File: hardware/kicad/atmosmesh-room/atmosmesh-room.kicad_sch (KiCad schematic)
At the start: 32 parts, among them U1 IDEASPARK_ESP32_1V14_TFT_30PIN

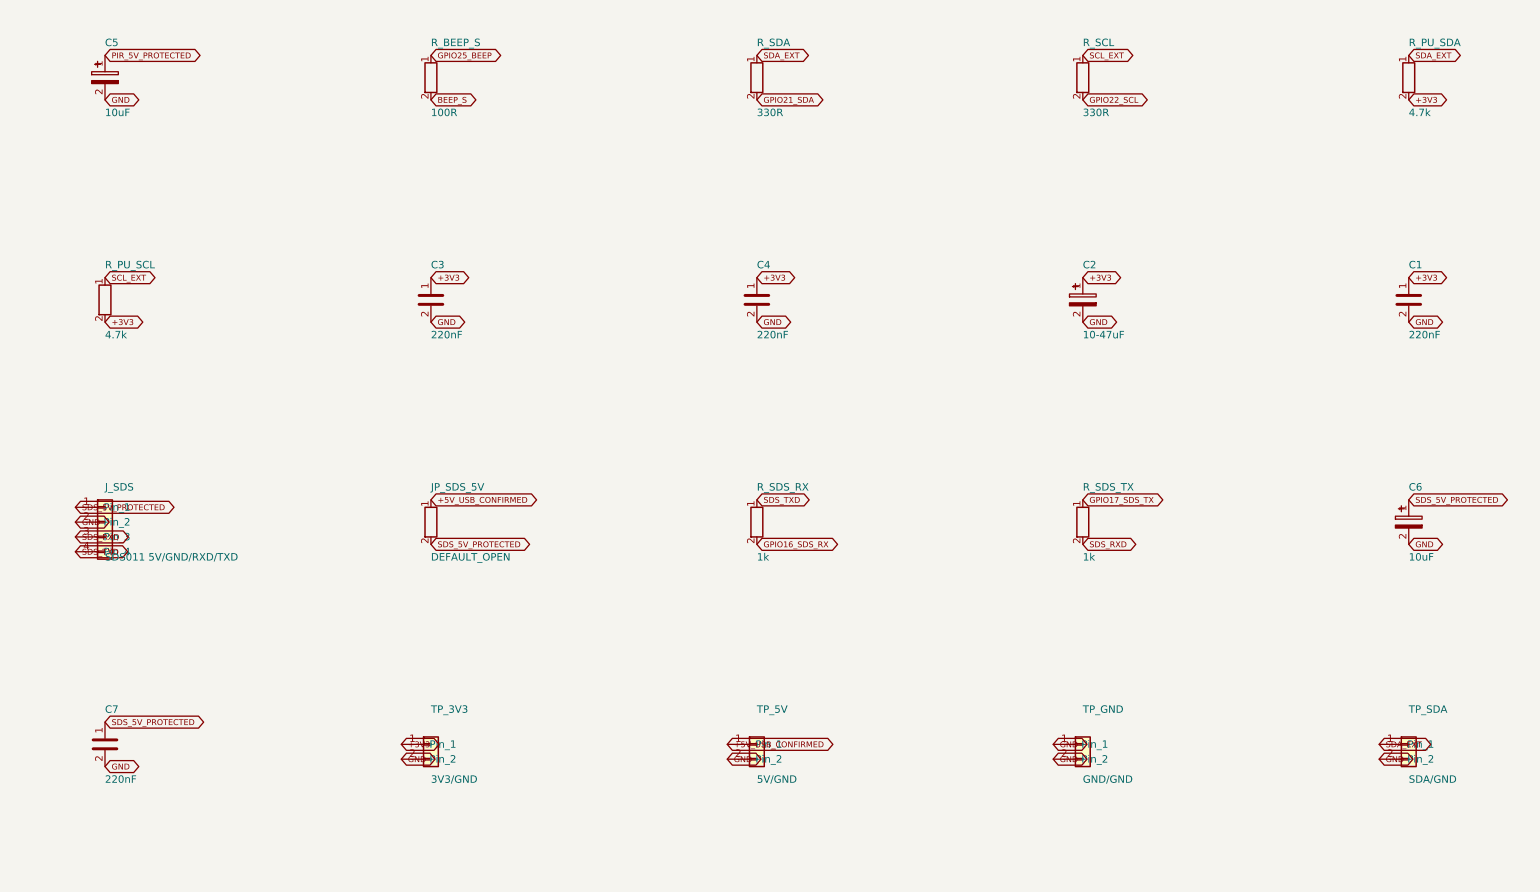
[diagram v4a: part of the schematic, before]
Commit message: :sparkles: feat(room): build on the perfboard and with the parts that exist
ROOM-03 and ROOM-04. The operator solders this by hand on a 31x27 perfboard and
does not need the PCB, and the inventory landed in the repo, so several values
that were chosen "because those parts are available" no longer have to be.

Perfboard becomes the build target (D-027):

- perfboard.md carries the grid facts, placement zones, hole budget and build
  order. The 7x9 cm label and the 31x27 hole count are reconciled: the extra
  millimetres are unholed lead-in strips.
- validate_room_perfboard.py gates it. A build plan with no gate is exactly the
  pattern this repo keeps hitting. All five assertions are mutation-proved.
- Step 1 is a dry-fit. 25.4 mm is exactly 10 pitches, so counting holes settles
  the row spacing that has blocked D-024 since the design started.
- The principal new hazard is orientation: the pinout sheet is a top view and
  soldering happens from the copper side, where left and right invert. Two
  connector orders were already found reversed here, so the wiring table is
  authoritative by pin NAME and the validator refuses to let that warning go.
- atmosmesh-room.kicad_pcb is parked, not deleted. It still cross-checks nets
  and silkscreen; it is not a fabrication candidate.

Values, now that stock is known:

- Pull-ups 4.7k -> 3.3k. Rise time binds on hand-wired perfboard: at 100 kHz
  I2C allows 1000 ns and 4.7k against ~200 pF gives 940 ns, on the limit. 3.3k
  gives 660 ns. wiring.md gains a table justifying every resistor; the operator
  holds a full E24 kit, so none of them is a stock compromise.
- C6 10uF -> 470uF. Its ripple limit is 20 mV against a fan and 10 uF was never
  shown to meet it. C5 and C2 -> 100uF. Electrolytics run to 1000 uF.
- Ceramics go the other way: 220nF -> 100nF for C1/C3/C4/C7, because the
  ceramic assortment stops at 100 nF and D-022 already allowed 47-220 nF.
- Closing JP_SDS_5V now has an ordering rule: before USB power, not while l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
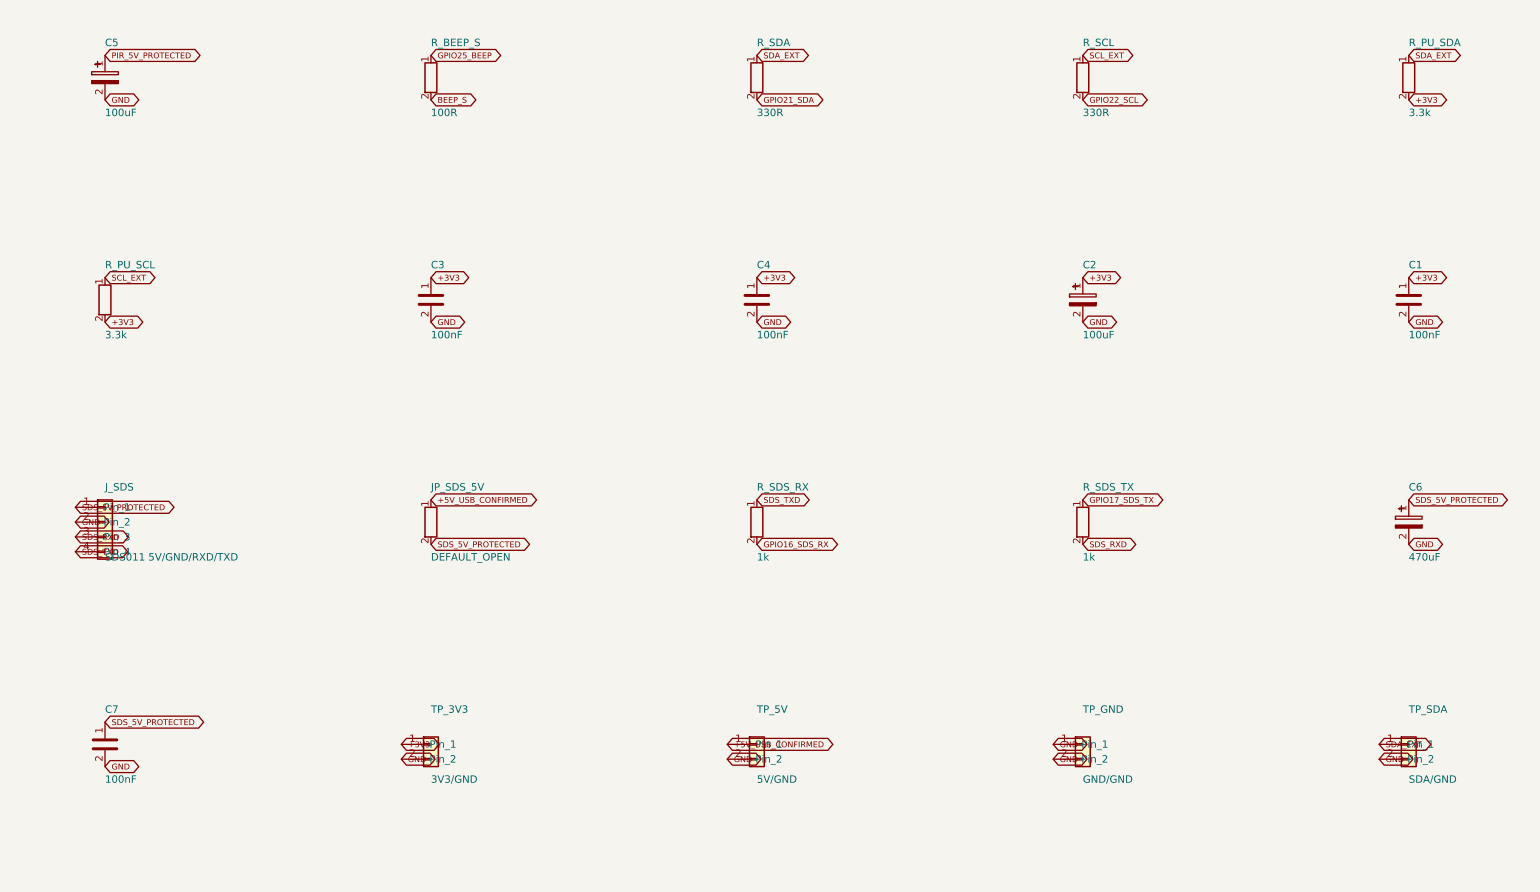
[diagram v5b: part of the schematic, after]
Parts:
- C1, C3, C4, C7: value 220nF -> 100nF
- C2: value 10-47uF -> 100uF
- C5: value 10uF -> 100uF
- C6: value 10uF -> 470uF
- R_PU_SCL, R_PU_SDA: value 4.7k -> 3.3k
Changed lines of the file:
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@@
       (effects (font (size 1.27 1.27)) (justify left))
     )
-    (property "Value" "10uF" (at 142.24 127.92 0)
+    (property "Value" "100uF" (at 142.24 127.92 0)
       (effects (font (size 1.27 1.27)) (justify left))
     )
@@
       (effects (font (size 1.27 1.27)) hide)
     )
-    (property "Description" "10 uF protected PIR 5V bulk capacitor; observe polarity" (at 142.24 121.92 0)
+    (property "Description" "100 uF protected PIR 5V bulk capacitor; observe polarity" (at 142.24 121.92 0)
       (effects (font (size 1.27 1.27)) hide)
     )
@@
       (effects (font (size 1.27 1.27)) (justify left))
     )
-    (property "Value" "4.7k" (at 365.76 127.92 0)
+    (property "Value" "3.3k" (at 365.76 127.92 0)
       (effects (font (size 1.27 1.27)) (justify left))
     )
@@
       (effects (font (size 1.27 1.27)) hide)
     )
-    (property "Description" "4.7 kilohm SDA_EXT pullup to 3V3; the TFT board has no onboard I2C pullups" (at 365.76 121.92 0)
+    (property "Description" "3.3 kilohm SDA_EXT pullup to 3V3; sized for perfboard wiring capacitance at 100 kHz" (at 365.76 121.92 0)
       (effects (font (size 1.27 1.27)) hide)
     )
@@
       (effects (font (size 1.27 1.27)) (justify left))
     )
-    (property "Value" "4.7k" (at 142.24 166.02 0)
+    (property "Value" "3.3k" (at 142.24 166.02 0)
       (effects (font (size 1.27 1.27)) (justify left))
     )
@@
       (effects (font (size 1.27 1.27)) hide)
     )
-    (property "Description" "4.7 kilohm SCL_EXT pullup to 3V3; the TFT board has no onboard I2C pullups" (at 142.24 160.02 0)
+    (property "Description" "3.3 kilohm SCL_EXT pullup to 3V3; sized for perfboard wiring capacitance at 100 kHz" (at 142.24 160.02 0)
       (effects (font (size 1.27 1.27)) hide)
     )
@@
       (effects (font (size 1.27 1.27)) (justify left))
     )
-    (property "Value" "220nF" (at 198.12 166.02 0)
+    (property "Value" "100nF" (at 198.12 166.02 0)
       (effects (font (size 1.27 1.27)) (justify left))
     )
@@
       (effects (font (size 1.27 1.27)) hide)
     )
-    (property "Description" "220 nF VEML7700 VIN input decoupling; 47-220 nF acceptable" (at 198.12 160.02 0)
+    (property "Description" "100 nF VEML7700 VIN input decoupling" (at 198.12 160.02 0)
       (effects (font (size 1.27 1.27)) hide)
     )
@@
       (effects (font (size 1.27 1.27)) (justify left))
     )
-    (property "Value" "220nF" (at 254.0 166.02 0)
+    (property "Value" "100nF" (at 254.0 166.02 0)
       (effects (font (size 1.27 1.27)) (justify left))
     )
@@
       (effects (font (size 1.27 1.27)) hide)
     )
-    (property "Description" "220 nF SHT41 3V3 local decoupling; 47-220 nF acceptable" (at 254.0 160.02 0)
+    (property "Description" "100 nF SHT41 3V3 local decoupling" (at 254.0 160.02 0)
       (effects (font (size 1.27 1.27)) hide)
     )
@@
       (effects (font (size 1.27 1.27)) (justify left))
     )
-    (property "Value" "10-47uF" (at 309.88 166.02 0)
+    (property "Value" "100uF" (at 309.88 166.02 0)
       (effects (font (size 1.27 1.27)) (justify left))
     )
@@
       (effects (font (size 1.27 1.27)) hide)
     )
-    (property "Description" "10-47 uF controller 3V3 bulk capacitor; observe polarity" (at 309.88 160.02 0)
+    (property "Description" "100 uF controller 3V3 bulk capacitor; observe polarity" (at 309.88 160.02 0)
       (effects (font (size 1.27 1.27)) hide)
     )
@@
       (effects (font (size 1.27 1.27)) (justify left))
     )
-    (property "Value" "220nF" (at 365.76 166.02 0)
+    (property "Value" "100nF" (at 365.76 166.02 0)
       (effects (font (size 1.27 1.27)) (justify left))
     )
@@
       (effects (font (size 1.27 1.27)) hide)
     )
-    (property "Description" "220 nF controller 3V3 local decoupling; 47-220 nF acceptable" (at 365.76 160.02 0)
+    (property "Description" "100 nF controller 3V3 local decoupling" (at 365.76 160.02 0)
       (effects (font (size 1.27 1.27)) hide)
     )
@@
       (effects (font (size 1.27 1.27)) (justify left))
     )
-    (property "Value" "10uF" (at 365.76 204.12 0)
+    (property "Value" "470uF" (at 365.76 204.12 0)
       (effects (font (size 1.27 1.27)) (justify left))
     )
@@
       (effects (font (size 1.27 1.27)) hide)
     )
-    (property "Description" "10 uF protected SDS011 5V bulk capacitor; observe polarity" (at 365.76 198.12 0)
+    (property "Description" "470 uF protected SDS011 5V bulk; sized for the fan against the 20 mV ripple limit; observe polarity" (at 365.76 198.12 0)
       (effects (font (size 1.27 1.27)) hide)
     )
@@
       (effects (font (size 1.27 1.27)) (justify left))
     )
-    (property "Value" "220nF" (at 142.24 242.22 0)
+    (property "Value" "100nF" (at 142.24 242.22 0)
       (effects (font (size 1.27 1.27)) (justify left))
     )
@@
       (effects (font (size 1.27 1.27)) hide)
     )
-    (property "Description" "220 nF SDS011 5V high-frequency decoupling" (at 142.24 236.22 0)
-      (effects (font (size 1.27 1.27)) hide)
-    )
+    (property "Description" "100 nF SDS011 5V high-frequency decoupling" (at 142.24 236.22 0)
+      (effects (font (size 1.27 1.27)) hide)
+    )
